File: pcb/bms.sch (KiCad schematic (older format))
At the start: 15 parts, among them J10 Taps 6-8, J11 Taps 0-5, J12 Taps 6-8, J13 Taps 0-5, J14 USB_B_Mini

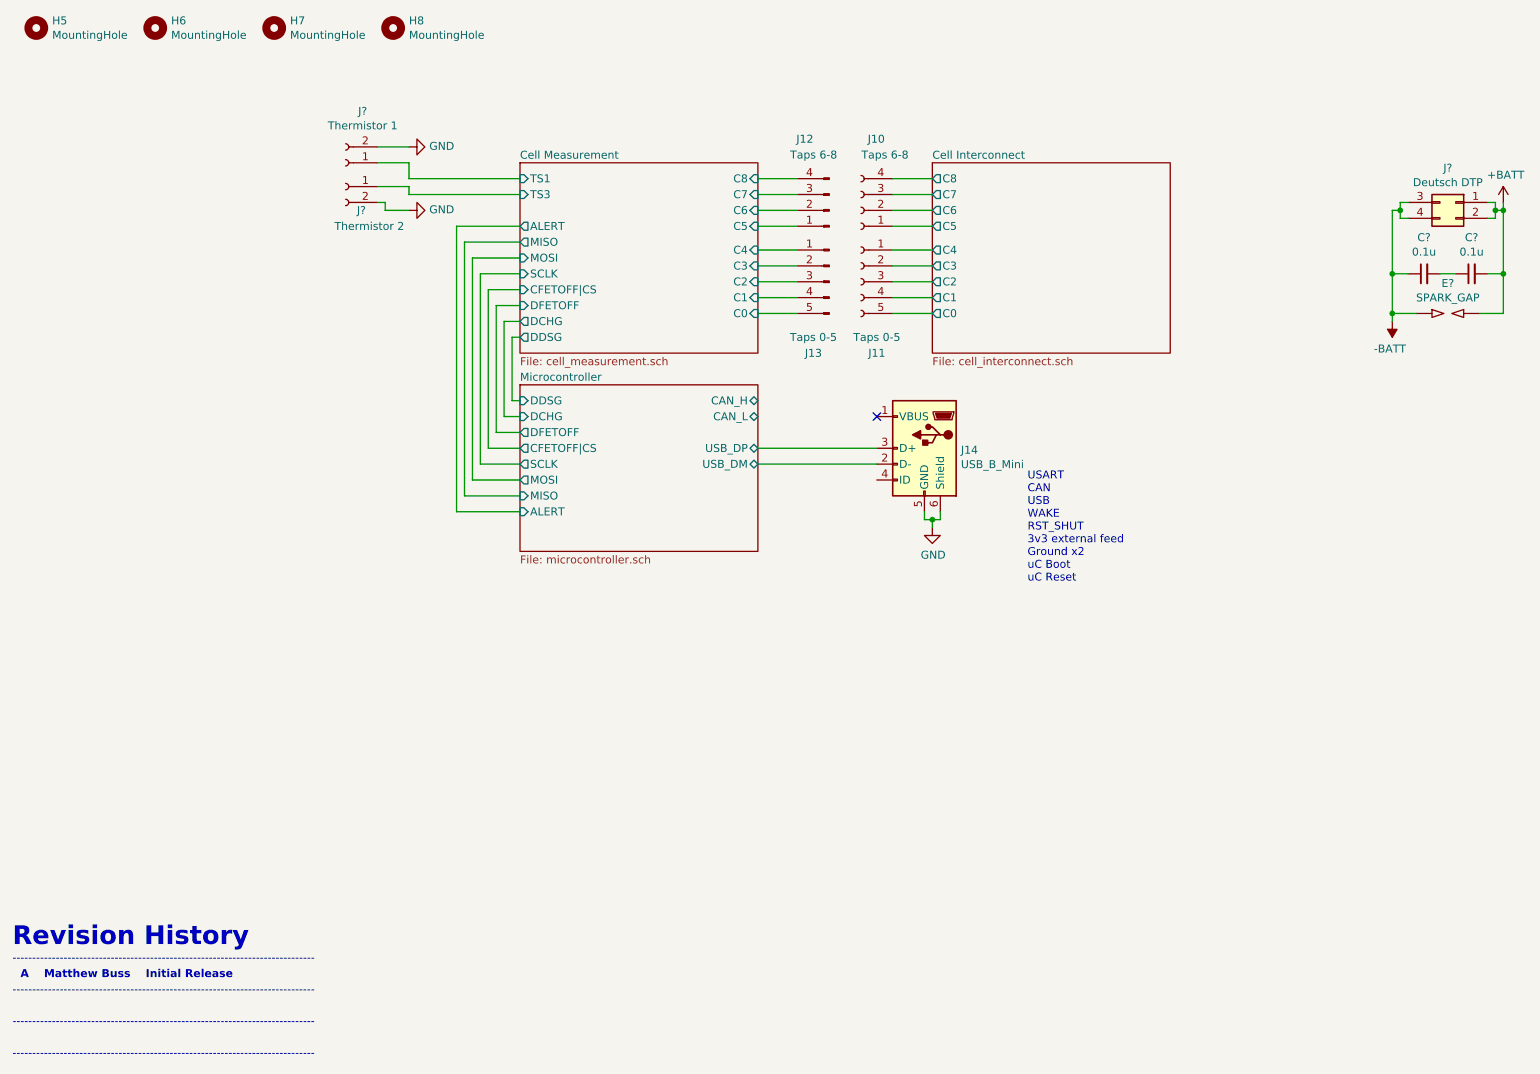
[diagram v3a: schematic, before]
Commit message: microcontroller added
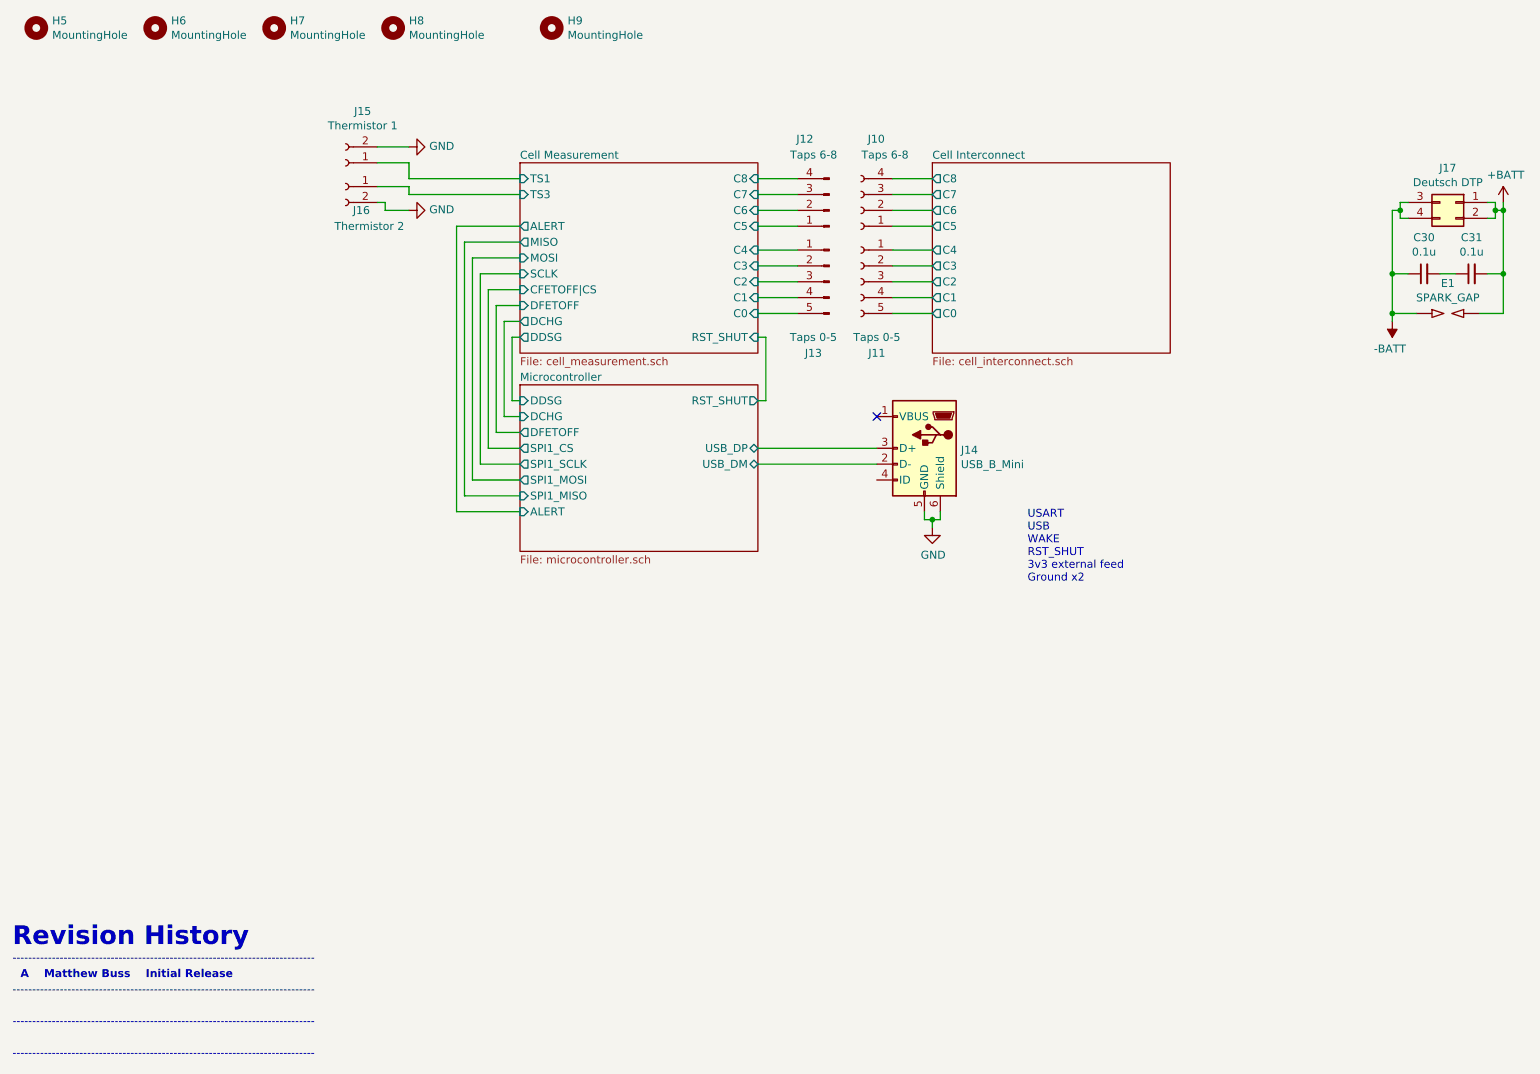
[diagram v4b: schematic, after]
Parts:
- added H9: MountingHole, MountingHole:MountingHole_3.2mm_M3, symbol Mechanical:MountingHole
- C30, C31: renamed from C?; footprint (none) -> Capacitor_SMD:C_0805_2012Metric
- gave numbers to parts that had none: 4
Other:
- note added: "USART\nUSB\nWAKE\nRST_SHUT\n3v3 external feed\nGround x2"
- note removed: "USART\nCAN\nUSB\nWAKE\nRST_SHUT\n3v3 external feed\nGround x2\nuC Boot\nuC Reset"
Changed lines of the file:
@@
 F0 "Microcontroller" 50
 F1 "microcontroller.sch" 50
-F2 "CAN_H" B R 5200 3000 50
-F3 "CAN_L" B R 5200 3100 50
-F4 "USB_DP" B R 5200 3300 50
-F5 "USB_DM" B R 5200 3400 50
-F6 "ALERT" I L 3700 3700 50
-F7 "MISO" I L 3700 3600 50
-F8 "MOSI" O L 3700 3500 50
-F9 "SCLK" O L 3700 3400 50
-F10 "CFETOFF|CS" O L 3700 3300 50
-F11 "DFETOFF" O L 3700 3200 50
-F12 "DCHG" I L 3700 3100 50
-F13 "DDSG" I L 3700 3000 50
+F2 "USB_DP" B R 5200 3300 50
+F3 "USB_DM" B R 5200 3400 50
+F4 "DCHG" I L 3700 3100 50
+F5 "DDSG" I L 3700 3000 50
+F6 "DFETOFF" O L 3700 3200 50
+F7 "SPI1_CS" O L 3700 3300 50
+F8 "SPI1_SCLK" O L 3700 3400 50
+F9 "SPI1_MOSI" O L 3700 3500 50
+F10 "SPI1_MISO" I L 3700 3600 50
+F11 "ALERT" I L 3700 3700 50
+F12 "RST_SHUT" O R 5200 3000 50
 $EndSheet
 $Sheet
@@
 F19 "DCHG" O L 3700 2500 50
 F20 "DDSG" O L 3700 2600 50
+F21 "RST_SHUT" I R 5200 2600 50
 $EndSheet
 Wire Wire Line
@@
 NoConn ~ 5950 3100
 $Comp
-L Connector_Generic:Conn_02x02_Top_Bottom J?
+L Connector_Generic:Conn_02x02_Top_Bottom J17
 U 1 1 608EF286
 P 9600 1750
-F 0 "J?" H 9650 1967 50  0000 C CNN
+F 0 "J17" H 9650 1967 50  0000 C CNN
 F 1 "Deutsch DTP" H 9650 1876 50  0000 C CNN
 F 2 "" H 9600 1750 50  0001 C CNN
@@
 $EndComp
 Text Notes 6900 4150 0    50   ~ 0
-USART\nCAN\nUSB\nWAKE\nRST_SHUT\n3v3 external feed\nGround x2\nuC Boot\nuC Reset
+USART\nUSB\nWAKE\nRST_SHUT\n3v3 external feed\nGround x2
 Wire Wire Line
 	9800 1850 9850 1850
@@
 	9250 1800 9250 1850
 $Comp
-L power:+BATT #PWR?
+L power:+BATT #PWR05
 U 1 1 60DA1FD4
 P 9900 1750
-F 0 "#PWR?" H 9900 1600 50  0001 C CNN
+F 0 "#PWR05" H 9900 1600 50  0001 C CNN
 F 1 "+BATT" H 9915 1923 50  0000 C CNN
 F 2 "" H 9900 1750 50  0001 C CNN
@@
 $EndComp
 $Comp
-L power:-BATT #PWR?
+L power:-BATT #PWR04
 U 1 1 60DA2F2B
 P 9200 2500
-F 0 "#PWR?" H 9200 2350 50  0001 C CNN
+F 0 "#PWR04" H 9200 2350 50  0001 C CNN
 F 1 "-BATT" H 9215 2673 50  0000 C CNN
 F 2 "" H 9200 2500 50  0001 C CNN
@@
 $EndComp
 $Comp
-L Device:C_Small C?
+L Device:C_Small C31
 U 1 1 60E2A088
 P 9700 2200
-F 0 "C?" V 9929 2200 50  0000 C CNN
+F 0 "C31" V 9929 2200 50  0000 C CNN
 F 1 "0.1u" V 9838 2200 50  0000 C CNN
-F 2 "" H 9700 2200 50  0001 C CNN
+F 2 "Capacitor_SMD:C_0805_2012Metric" H 9700 2200 50  0001 C CNN
 F 3 "~" H 9700 2200 50  0001 C CNN
 	1    9700 2200
@@
 $EndComp
 $Comp
-L Device:C_Small C?
+L Device:C_Small C30
 U 1 1 60E2A775
 P 9400 2200
-F 0 "C?" V 9629 2200 50  0000 C CNN
+F 0 "C30" V 9629 2200 50  0000 C CNN
 F 1 "0.1u" V 9538 2200 50  0000 C CNN
-F 2 "" H 9400 2200 50  0001 C CNN
+F 2 "Capacitor_SMD:C_0805_2012Metric" H 9400 2200 50  0001 C CNN
 F 3 "~" H 9400 2200 50  0001 C CNN
 	1    9400 2200
@@
 	9900 1800 9900 1750
 $Comp
-L Device:SPARK_GAP E?
+L Device:SPARK_GAP E1
 U 1 1 60E2F095
 P 9550 2450
-F 0 "E?" H 9550 2640 50  0000 C CNN
+F 0 "E1" H 9550 2640 50  0000 C CNN
 F 1 "SPARK_GAP" H 9550 2549 50  0000 C CNN
 F 2 "" H 9550 2380 50  0001 C CNN
@@
 Connection ~ 9200 2450
 $Comp
-L Connector:Conn_01x02_Female J?
+L Connector:Conn_01x02_Female J15
 U 1 1 6110005E
 P 2600 1500
-F 0 "J?" H 2492 1175 50  0000 C CNN
+F 0 "J15" H 2492 1175 50  0000 C CNN
 F 1 "Thermistor 1" H 2492 1266 50  0000 C CNN
 F 2 "" H 2600 1500 50  0001 C CNN
@@
 $EndComp
 $Comp
-L Connector:Conn_01x02_Female J?
+L Connector:Conn_01x02_Female J16
 U 1 1 61101B81
 P 2600 1650
-F 0 "J?" H 2500 1500 50  0000 C CNN
+F 0 "J16" H 2500 1500 50  0000 C CNN
 F 1 "Thermistor 2" H 2450 1400 50  0000 C CNN
 F 2 "" H 2600 1650 50  0001 C CNN
@@
 	2800 1400 3000 1400
 $Comp
-L power:GND #PWR?
+L power:GND #PWR02
 U 1 1 6110DF10
 P 3000 1400
-F 0 "#PWR?" H 3000 1150 50  0001 C CNN
+F 0 "#PWR02" H 3000 1150 50  0001 C CNN
 F 1 "GND" V 3005 1272 50  0000 R CNN
 F 2 "" H 3000 1400 50  0001 C CNN
@@
 $EndComp
 $Comp
-L power:GND #PWR?
+L power:GND #PWR03
 U 1 1 6110E16F
 P 3000 1800
-F 0 "#PWR?" H 3000 1550 50  0001 C CNN
+F 0 "#PWR03" H 3000 1550 50  0001 C CNN
 F 1 "GND" V 3005 1672 50  0000 R CNN
 F 2 "" H 3000 1800 50  0001 C CNN
@@
 Wire Wire Line
 	3300 3700 3700 3700
+$Comp
+L Mechanical:MountingHole H?
+U 1 1 60925370
+P 3900 650
+AR Path="/607E490C/60925370" Ref="H?"  Part="1"
+AR Path="/60925370" Ref="H9"  Part="1"
+F 0 "H9" H 4000 696 50  0000 L CNN
+F 1 "MountingHole" H 4000 605 50  0000 L CNN
+F 2 "MountingHole:MountingHole_3.2mm_M3" H 3900 650 50  0001 C CNN
+F 3 "~" H 3900 650 50  0001 C CNN
+	1    3900 650
+	1    0    0    -1
+$EndComp
+Wire Wire Line
+	5200 3000 5250 3000
+Wire Wire Line
+	5250 3000 5250 2600
+Wire Wire Line
+	5250 2600 5200 2600
 $EndSCHEMATC
